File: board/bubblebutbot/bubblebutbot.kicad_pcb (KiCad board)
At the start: 2 copper layers, 30 x 70 mm, 32 parts, among them J1 Screw_Terminal_01x04, J2 Screw_Terminal_01x04, J3 Conn_01x06_Female, J4 Conn_01x06_Female, Q1 FDN336P, U1 WeMos_D1_mini, U3 TPS613222ADBV

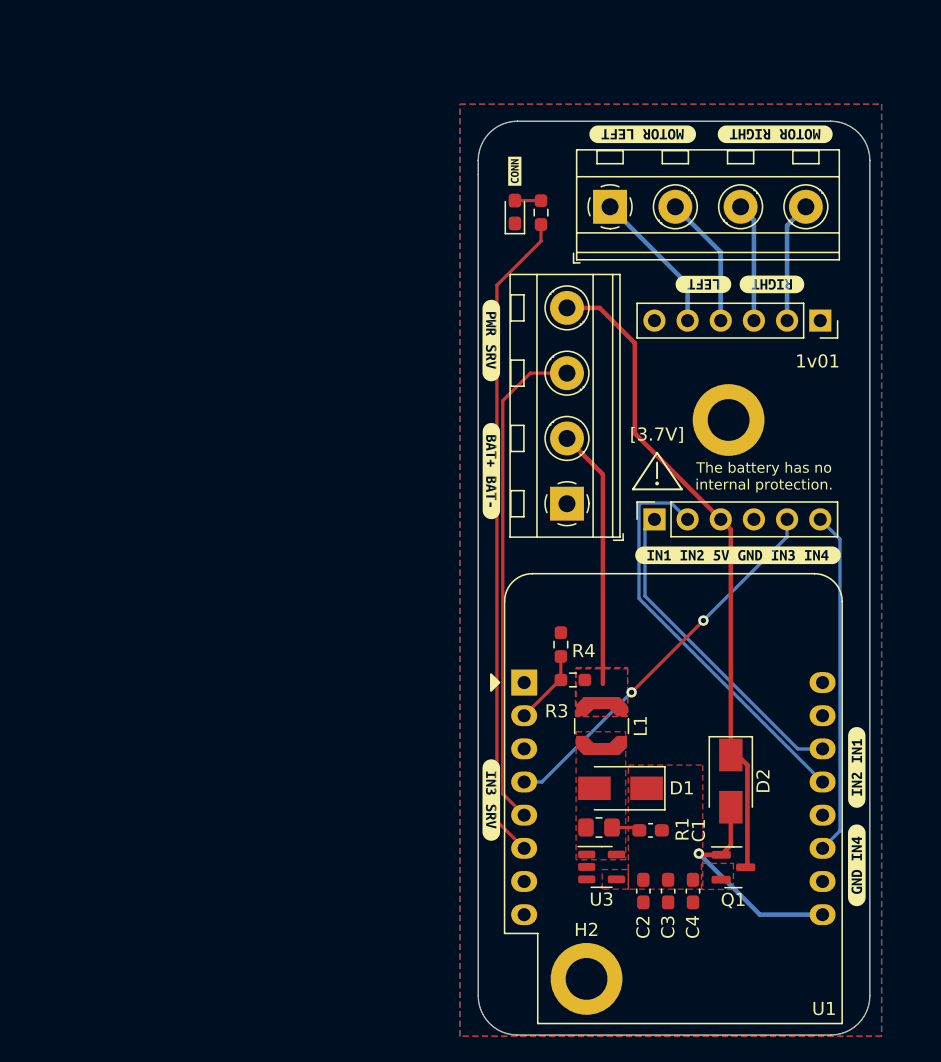
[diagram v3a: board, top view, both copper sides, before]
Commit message: finished schematic and BOM. Design is ready to start!
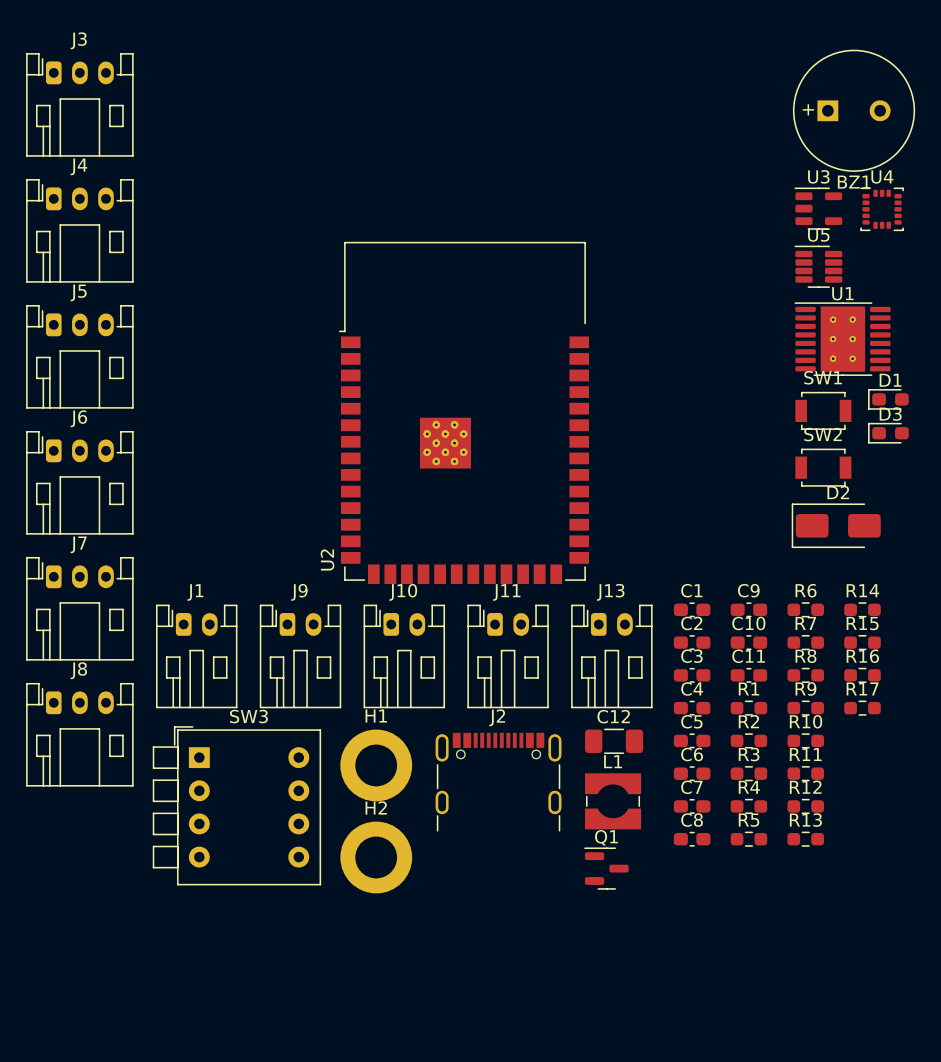
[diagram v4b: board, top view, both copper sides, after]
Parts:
- removed kibuzzard-641EE450: G***, kibuzzard-641EE450
- removed kibuzzard-641EE46F: G***, kibuzzard-641EE46F
- removed kibuzzard-641EE492: G***, kibuzzard-641EE492
- removed kibuzzard-641EE4C6: G***, kibuzzard-641EE4C6
- removed kibuzzard-641EE536: G***, kibuzzard-641EE536
- removed kibuzzard-641EE568: G***, kibuzzard-641EE568
- removed kibuzzard-641EE5F8: G***, kibuzzard-641EE5F8
- removed kibuzzard-641EE609: G***, kibuzzard-641EE609
- removed kibuzzard-641EE6B8: G***, kibuzzard-641EE6B8
- removed kibuzzard-641EE6C6: G***, kibuzzard-641EE6C6
- removed kibuzzard-641EE74D: G***, kibuzzard-641EE74D
- added BZ1: Buzzer, Buzzer_Beeper:MagneticBuzzer_PUI_AT-0927-TT-6-R, F.Cu at (177.8, 73.2)
- added C10: 10u, Capacitor_SMD:C_0603_1608Metric_Pad1.08x0.95mm_HandSolder, F.Cu at (171.7, 113.9)
- added C11: 100n, Capacitor_SMD:C_0603_1608Metric_Pad1.08x0.95mm_HandSolder, F.Cu at (171.7, 116.5)
- added C12: 22u, Capacitor_SMD:C_1206_3216Metric_Pad1.33x1.80mm_HandSolder, F.Cu at (161.4, 121.5)
- added C5: 1u, Capacitor_SMD:C_0603_1608Metric_Pad1.08x0.95mm_HandSolder, F.Cu at (167.4, 121.5)
- added C6: 100n, Capacitor_SMD:C_0603_1608Metric_Pad1.08x0.95mm_HandSolder, F.Cu at (167.4, 124.0)
- added C7: 2.2u, Capacitor_SMD:C_0603_1608Metric_Pad1.08x0.95mm_HandSolder, F.Cu at (167.4, 126.5)
- added C8: 100n, Capacitor_SMD:C_0603_1608Metric_Pad1.08x0.95mm_HandSolder, F.Cu at (167.4, 129.0)
- added C9: 10u, Capacitor_SMD:C_0603_1608Metric_Pad1.08x0.95mm_HandSolder, F.Cu at (171.7, 111.4)
- added J10: JST XH, Connector_JST:JST_PH_S2B-PH-K_1x02_P2.00mm_Horizontal, F.Cu at (144.3, 112.5)
- added J11: JST XH, Connector_JST:JST_PH_S2B-PH-K_1x02_P2.00mm_Horizontal, F.Cu at (152.3, 112.5)
- added J13: JST XH, Connector_JST:JST_PH_S2B-PH-K_1x02_P2.00mm_Horizontal, F.Cu at (160.2, 112.5)
- added J5: Conn_01x03_Socket, Connector_JST:JST_PH_S3B-PH-K_1x03_P2.00mm_Horizontal, F.Cu at (118.5, 89.6)
- added J6: Conn_01x03_Socket, Connector_JST:JST_PH_S3B-PH-K_1x03_P2.00mm_Horizontal, F.Cu at (118.5, 99.2)
- added J7: Conn_01x03_Socket, Connector_JST:JST_PH_S3B-PH-K_1x03_P2.00mm_Horizontal, F.Cu at (118.5, 108.9)
- added J8: Conn_01x03_Socket, Connector_JST:JST_PH_S3B-PH-K_1x03_P2.00mm_Horizontal, F.Cu at (118.5, 118.5)
- added J9: JST XH, Connector_JST:JST_PH_S2B-PH-K_1x02_P2.00mm_Horizontal, F.Cu at (136.4, 112.5)
- added R10: 5.1K, Resistor_SMD:R_0603_1608Metric_Pad0.98x0.95mm_HandSolder, F.Cu at (176.1, 121.5)
- added R11: 50k, Resistor_SMD:R_0603_1608Metric_Pad0.98x0.95mm_HandSolder, F.Cu at (176.1, 124.0)
- added R12: 5.1K, Resistor_SMD:R_0603_1608Metric_Pad0.98x0.95mm_HandSolder, F.Cu at (176.1, 126.5)
- added R13: 5.1K, Resistor_SMD:R_0603_1608Metric_Pad0.98x0.95mm_HandSolder, F.Cu at (176.1, 129.0)
- added R14: 100k, Resistor_SMD:R_0603_1608Metric_Pad0.98x0.95mm_HandSolder, F.Cu at (180.4, 111.4)
- added R15: 100k, Resistor_SMD:R_0603_1608Metric_Pad0.98x0.95mm_HandSolder, F.Cu at (180.4, 113.9)
- added R16: R, Resistor_SMD:R_0603_1608Metric_Pad0.98x0.95mm_HandSolder, F.Cu at (180.4, 116.5)
- added R17: 5.1K, Resistor_SMD:R_0603_1608Metric_Pad0.98x0.95mm_HandSolder, F.Cu at (180.4, 119.0)
- added R5: 3.3k, Resistor_SMD:R_0603_1608Metric_Pad0.98x0.95mm_HandSolder, F.Cu at (171.7, 129.0)
- added R6: 5.1K, Resistor_SMD:R_0603_1608Metric_Pad0.98x0.95mm_HandSolder, F.Cu at (176.1, 111.4)
- added R7: 5.1K, Resistor_SMD:R_0603_1608Metric_Pad0.98x0.95mm_HandSolder, F.Cu at (176.1, 113.9)
- added R8: 100k, Resistor_SMD:R_0603_1608Metric_Pad0.98x0.95mm_HandSolder, F.Cu at (176.1, 116.5)
- added R9: 5.1K, Resistor_SMD:R_0603_1608Metric_Pad0.98x0.95mm_HandSolder, F.Cu at (176.1, 119.0)
- added SW1: SW_Push, Button_Switch_SMD:SW_SPST_B3U-1000P, F.Cu at (177.4, 96.2)
- added SW2: SW_Push, Button_Switch_SMD:SW_SPST_B3U-1000P, F.Cu at (177.4, 100.5)
- added SW3: SW_DIP_x04, Button_Switch_THT:SW_DIP_SPSTx04_Piano_10.8x11.72mm_W7.62mm_P2.54mm, F.Cu at (129.6, 122.8)
- added U2: ESP32-S3-WROOM-1, RF_Module:ESP32-S3-WROOM-1, F.Cu at (150.0, 96.2)
- added U4: LIS3DH, Package_LGA:LGA-16_3x3mm_P0.5mm_LayoutBorder3x5y, F.Cu at (181.9, 80.8)
- added U5: ~, Package_TO_SOT_SMD:SOT-23-8, F.Cu at (177.1, 85.2)
- C1: value 120p -> 10u
- C4: value 10u -> 1u
- D1: value SS14 -> LED; footprint Diode_SMD:D_SMA -> LED_SMD:LED_0603_1608Metric_Pad1.05x0.95mm_HandSolder
- J1: value Screw_Terminal_01x04 -> JST XH; footprint TerminalBlock_MetzConnect:TerminalBlock_MetzConnect_Type094_RT03504HBLU_1x04_P5.00mm_Horizontal -> Connector_JST:JST_PH_S2B-PH-K_1x02_P2.00mm_Horizontal
- J2: value Screw_Terminal_01x04 -> USB_C_Receptacle; footprint TerminalBlock_MetzConnect:TerminalBlock_MetzConnect_Type094_RT03504HBLU_1x04_P5.00mm_Horizontal -> Connector_USB:USB_C_Receptacle_GCT_USB4105-xx-A_16P_TopMnt_Horizontal
- J3, J4: value Conn_01x06_Female -> Conn_01x03_Socket; footprint Connector_PinSocket_2.54mm:PinSocket_1x06_P2.54mm_Vertical -> Connector_JST:JST_PH_S3B-PH-K_1x03_P2.00mm_Horizontal
- L1: value 2.2u -> 4.7u; footprint Inductor_SMD:L_Coilcraft_LPS4018 -> Inductor_SMD:L_Wuerth_WE-TPC-3816
- R1: value 5 -> 5.1K; footprint Resistor_SMD:R_0805_2012Metric_Pad1.20x1.40mm_HandSolder -> Resistor_SMD:R_0603_1608Metric_Pad0.98x0.95mm_HandSolder
- R2: value 1k -> 5.1K
- R3: value 10k -> 5.1K
- R4: value 33k -> 5.1K
- U1: value WeMos_D1_mini -> DRV8833PWP; footprint Module:WEMOS_D1_mini_light -> Package_SO:HTSSOP-16-1EP_4.4x5mm_P0.65mm_EP3.4x5mm_Mask2.46x2.31mm_ThermalVias
- U3: value TPS613222ADBV -> AP2112K-3.3
- moved J3 61.7 mm to (118.5, 70.3), turned to 0 degrees
- moved U3 53.1 mm to (177.1, 80.7)
- moved J4 52.2 mm to (118.5, 80.0), turned to 0 degrees
- moved J2 45.4 mm to (152.6, 125.1)
- moved R2 43.5 mm to (171.7, 121.5), turned to 0 degrees
- moved H1 37.8 mm to (143.2, 123.3)
- moved D1 36.3 mm to (182.6, 95.3), turned to 0 degrees
- moved U1 35.9 mm to (178.9, 90.7)
- moved D3 33.4 mm to (182.6, 97.9), turned to 0 degrees
- moved J1 30.8 mm to (128.4, 112.5), turned to 0 degrees
- moved D2 21.2 mm to (178.6, 105.0), turned to 0 degrees
- moved C2 19.4 mm to (167.4, 113.9), turned to 0 degrees
- moved R4 19.0 mm to (171.7, 126.5), turned to 0 degrees
- moved H2 18.6 mm to (143.2, 130.4)
- moved C1 17.2 mm to (167.4, 111.4)
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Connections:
- C1 pad 1: Net-(C1-Pad1) -> +3.3V
- C1 pad 2: Net-(C1-Pad2) -> GND
- C2 pad 1: Net-(C1-Pad2) -> +3.3V
- C3 pad 1: Net-(C1-Pad2) -> ESP32-RESET
- C4 pad 1: Net-(C1-Pad2) -> +3.3V
- D1 pad 1: Net-(C1-Pad2) -> GND
- D1 pad 2: Net-(D1-Pad2) -> Net-(D1-A)
- D2 pad 1: SPLY -> +5V
- D2 pad 2: WEMOS_USB_POWER -> 5V_USB_POWER
- D3 pad 2: Net-(D3-Pad2) -> Net-(D3-A)
- J1 pad 2: Net-(L1-Pad1) -> +7.5V
- J3 pad 1: unconnected-(J3-Pad1) -> GND
- J3 pad 2: Net-(J3-Pad2) -> ESP32-IR-FL
- J3 pad 3: Net-(J3-Pad3) -> +5V
- J4 pad 1: IN1 -> GND
- J4 pad 2: IN2 -> ESP32-IR-FR
- J4 pad 3: SPLY -> +5V
- L1 pad 1: Net-(L1-Pad1) -> Net-(U5-LX)
- L1 pad 2: Net-(D1-Pad2) -> 5V_BAT
- Q1 pad 1: WEMOS_USB_POWER -> 5V_USB_POWER
- Q1 pad 2: Net-(C1-Pad2) -> 5V_BAT
- Q1 pad 3: SPLY -> +5V
- R1 pad 1: Net-(D1-Pad2) -> +3.3V
- R1 pad 2: Net-(C1-Pad1) -> ESP32-RESET
- R2 pad 1: Net-(R2-Pad1) -> Net-(D1-A)
- R2 pad 2: Net-(D3-Pad2) -> ESP32-OP-LED
- R3 pad 1: Net-(L1-Pad1) -> Net-(R3-Pad1)
- R3 pad 2: BATTERY_LVL -> +3.3V
- R4 pad 1: BATTERY_LVL -> GND
- R4 pad 2: GND -> Net-(J2-CC1)
- U1 pad 1: unconnected-(U1-Pad1) -> Net-(U1-nSLEEP)
- U1 pad 10: GND -> ESP32-MOTOR-BIN2
- U1 pad 11: IN4 -> Net-(U1-VCP)
- U1 pad 12: unconnected-(U1-Pad12) -> 5V_SUPPLY
- U1 pad 13: IN2 -> GND
- U1 pad 14: IN1 -> Net-(U1-VINT)
- U1 pad 15: unconnected-(U1-Pad15) -> ESP32-MOTOR-AIN2
- U1 pad 16: unconnected-(U1-Pad16) -> ESP32-MOTOR-AIN1
- U1 pad 2: BATTERY_LVL -> MOTOR-RIGHT-BL
- U1 pad 3: unconnected-(U1-Pad3) -> GND
- U1 pad 4: IN3 -> MOTOR-RIGHT-BR
- U1 pad 5: SERVO_PWM -> MOTOR-LEFT-BR
- U1 pad 6: Net-(R2-Pad1) -> GND
- U1 pad 7: unconnected-(U1-Pad7) -> MOTOR-LEFT-BL
- U1 pad 8: unconnected-(U1-Pad8) -> ESP32-MOTOR-FAULT
- U1 pad 9: WEMOS_USB_POWER -> ESP32-MOTOR-BIN1
- U3 pad 1: Net-(D1-Pad2) -> +5V
- U3 pad 3: unconnected-(U3-Pad3) -> +5V
- U3 pad 4: Net-(C1-Pad2) -> unconnected-(U3-NC-Pad4)
- U3 pad 5: unconnected-(U3-Pad5) -> +3.3V
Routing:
- net SPLY: track 50.1 -> 0.00 mm
- net Net-(R2-Pad1): track 50.1 -> 0.00 mm
- net SERVO_PWM: track 38.2 -> 0.00 mm
- net IN2: track 31.4 -> 0.00 mm
- net IN3: track 29.3 -> 0.00 mm, vias 2 -> 0
- net IN4: track 26.4 -> 0.00 mm
- net IN1: track 24.6 -> 0.00 mm
- net Net-(L1-Pad1): track 19.9 -> 0.00 mm
- net WEMOS_USB_POWER: track 16.9 -> 0.00 mm, vias 1 -> 0
- net Net-(J3-Pad5): track 11.2 -> 0.00 mm
- net Net-(J3-Pad4): track 10.2 -> 0.00 mm
- net Net-(J3-Pad2): track 9.32 -> 0.00 mm
- net Net-(J3-Pad3): track 9.14 -> 0.00 mm
- net BATTERY_LVL: track 5.75 -> 0.00 mm
- net Net-(C1-Pad1): track 2.18 -> 0.00 mm
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- removed copper zone on B.Cu, net GND
- removed copper zone on F.Cu, net GND
- removed copper zone on F.Cu, net Net-(C1-Pad2)
- removed copper zone on F.Cu, net Net-(D1-Pad2)
- removed copper zone on F.Cu, net Net-(L1-Pad1)
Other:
- board outline removed
- board text removed: "1v01"
- board text removed: "The battery has no internal protection."
- board text removed: "[3.7V]"

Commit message: a few more improvements here and there. Almost there.
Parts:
- removed R3: 5.1K, Resistor_SMD:R_0603_1608Metric_Pad0.98x0.95mm_HandSolder
- removed SW3: SW_DIP_x04, Button_Switch_THT:SW_DIP_SPSTx04_Piano_10.8x11.72mm_W7.62mm_P2.54mm
- moved R17 140.8 mm to (72.4, 28.6)
- moved D3 133.5 mm to (68.5, 28.6)
- moved R4 129.7 mm to (77.1, 37.8), turned to 90 degrees
- moved R10 128.2 mm to (78.9, 37.8), turned to 90 degrees
- moved R13 128.0 mm to (76.6, 48.4), turned to 90 degrees
- moved R7 126.3 mm to (75.3, 37.8), turned to -90 degrees
- moved Q1 122.9 mm to (82.2, 36.9)
- moved J2 122.6 mm to (69.3, 35.1), turned to -90 degrees
- moved R15 122.5 mm to (81.2, 42.2), turned to 180 degrees
- moved R16 120.8 mm to (85.2, 42.2)
- moved R5 119.5 mm to (80.3, 52.0), turned to -90 degrees
- moved D2 119.0 mm to (83.8, 33.1), turned to 180 degrees
- moved L1 118.0 mm to (76.6, 43.9), turned to 180 degrees
- moved C5 117.6 mm to (88.5, 34.3), turned to -90 degrees
- moved H1 117.0 mm to (78.5, 25.8)
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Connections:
- R8 pad 2: +5V -> Net-(U3-EN)
- U2 pad 12: ESP32-SRV-F -> unconnected-(U2-GPIO8/TOUCH8/ADC1_CH7/SUBSPICS1-Pad12)
- U2 pad 18: ESP32-OP-LED -> ESP32-SRV-F
- U2 pad 19: ESP32-WIFI-ANALOG -> ESP32-OP-LED
- U2 pad 20: ESP32-MANUAL-AUTO -> ESP32-ACC-SDA
- U2 pad 21: ESP32-SERVO-EN -> ESP32-ACC-SCL
- U3 pad 3: +5V -> Net-(U3-EN)
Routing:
- net MOTOR-LEFT-BR: track 0.00 -> 15.5 mm, vias 0 -> 1
- net MOTOR-LEFT-BL: track 0.00 -> 15.1 mm
- net ESP32-ACC-INT1: track 0.00 -> 13.4 mm, vias 0 -> 2
- net ESP32-ACC-INT2: track 0.00 -> 12.3 mm, vias 0 -> 2
- net ESP32-ACC-SCL: track 0.00 -> 11.8 mm
- net ESP32-IR-BR: track 0.00 -> 10.8 mm, vias 0 -> 1
- net ESP32-IR-BL: track 0.00 -> 10.7 mm, vias 0 -> 1
- net ESP32-ACC-SDA: track 0.00 -> 10.1 mm
- net ESP32-IR-FL: track 0.00 -> 1.97 mm, vias 0 -> 1
- net ESP32-IR-FR: track 0.00 -> 1.97 mm, vias 0 -> 1
- added copper zone on F.Cu, net GND
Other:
- board outline added: 94 x 32.5 mm
- board text added: "power.bat"
- board text added: "power.usb"

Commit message: pcb done!
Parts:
- added kibuzzard-6507374A: G***, kibuzzard-6507374A, F.Cu at (115.5, 33.6)
- added kibuzzard-6507377B: G***, kibuzzard-6507377B, F.Cu at (124.0, 33.6)
- added kibuzzard-65073792: G***, kibuzzard-65073792, F.Cu at (133.6, 33.6)
- added kibuzzard-650737FA: G***, kibuzzard-650737FA, F.Cu at (143.0, 33.6)
- added kibuzzard-65073803: G***, kibuzzard-65073803, F.Cu at (151.5, 33.6)
- added kibuzzard-65073819: G***, kibuzzard-65073819, F.Cu at (115.5, 44.5)
- added kibuzzard-6507382A: G***, kibuzzard-6507382A, F.Cu at (124.0, 44.5)
- added kibuzzard-6507384E: G***, kibuzzard-6507384E, F.Cu at (133.5, 44.5)
- added kibuzzard-6507385B: G***, kibuzzard-6507385B, F.Cu at (143.0, 44.5)
- added kibuzzard-65073881: G***, kibuzzard-65073881, F.Cu at (151.5, 44.5)
- added kibuzzard-650738AB: G***, kibuzzard-650738AB, F.Cu at (135.3, 36.6)
- added kibuzzard-650739D2: G***, kibuzzard-650739D2, F.Cu at (69.3, 44.4)
- added kibuzzard-650739DD: G***, kibuzzard-650739DD, F.Cu at (66.4, 42.8)
- added kibuzzard-650739F6: G***, kibuzzard-650739F6, F.Cu at (66.3, 27.5)
- moved C1 43.1 mm to (108.8, 52.0), turned to -90 degrees
- moved D1 42.2 mm to (99.4, 28.1)
- moved R2 42.2 mm to (99.4, 31.8)
- moved U2 41.9 mm to (97.8, 47.4)
- moved C6 41.5 mm to (90.2, 27.1), turned to -90 degrees
- moved C2 41.4 mm to (110.6, 52.0), turned to -90 degrees
- moved R12 40.0 mm to (93.8, 27.1), turned to 90 degrees
- moved C10 39.8 mm to (92.0, 27.1), turned to -90 degrees
- moved U4 39.2 mm to (94.6, 31.6), turned to -90 degrees
- moved R9 35.2 mm to (95.6, 27.1)
- moved C3 33.3 mm to (122.8, 42.6), turned to -90 degrees
- moved R1 31.5 mm to (120.8, 42.6), turned to 90 degrees
- moved J10 28.6 mm to (116.5, 31.1)
- moved J13 28.6 mm to (152.5, 31.1)
- moved J3 28.6 mm to (126.0, 31.1)
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- renumbered SW2 to boot, SW1 to rst
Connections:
- C8 pad 2: 5V_SUPPLY -> +5V
- R11 pad 1: 5V_SUPPLY -> +5V
- U1 pad 12: 5V_SUPPLY -> +5V
- U2 pad 10: ESP32-MOTOR-AIN1 -> ESP32-SRV-B
- U2 pad 11: ESP32-MOTOR-AIN2 -> ESP32-SRV-F
- U2 pad 17: ESP32-SRV-B -> ESP32-MOTOR-AIN1
- U2 pad 18: ESP32-SRV-F -> ESP32-MOTOR-AIN2
- U2 pad 19: ESP32-OP-LED -> ESP32-MOTOR-BIN1
- U2 pad 20: ESP32-ACC-SDA -> ESP32-MOTOR-FAULT
- U2 pad 21: ESP32-ACC-SCL -> ESP32-OP-LED
- U2 pad 22: ESP32-MOTOR-FAULT -> ESP32-ACC-INT1
- U2 pad 23: ESP32-MOTOR-BIN1 -> ESP32-ACC-INT2
- U2 pad 24: ESP32-ACC-INT1 -> ESP32-ACC-SDA
- U2 pad 25: ESP32-ACC-INT2 -> ESP32-ACC-SCL
- U2 pad 4: ESP32-IR-FL -> ESP32-IR-BR
- U2 pad 5: ESP32-IR-FR -> ESP32-IR-BL
- U2 pad 6: ESP32-IR-BL -> ESP32-IR-FR
- U2 pad 7: ESP32-IR-BR -> ESP32-IR-FL
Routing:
- net +5V: track 0.00 -> 97.7 mm, vias 0 -> 5
- net ESP32-BUZZER: track 0.00 -> 70.4 mm, vias 0 -> 1
- net MOTOR-RIGHT-BL: track 0.00 -> 61.0 mm
- net MOTOR-RIGHT-BR: track 0.00 -> 60.7 mm
- net ESP32-D+: track 0.00 -> 46.8 mm, vias 0 -> 2
- net +3.3V: track 0.00 -> 45.9 mm, vias 0 -> 7
- net ESP32-BOOT0: track 0.00 -> 44.4 mm, vias 0 -> 2
- net ESP32-D-: track 0.00 -> 41.9 mm, vias 0 -> 2
- net ESP32-IR-FR: track 1.97 -> 42.6 mm, vias 1 -> 0
- net ESP32-SRV-F: track 0.00 -> 31.2 mm, vias 0 -> 1
- net ESP32-SRV-B: track 0.00 -> 30.0 mm, vias 0 -> 1
- net ESP32-IR-BR: track 10.8 -> 38.9 mm, vias 1 -> 2
- net ESP32-MOTOR-BIN2: track 0.00 -> 27.5 mm, vias 0 -> 2
- net ESP32-RESET: track 0.00 -> 25.1 mm, vias 0 -> 2
- net ESP32-IR-FL: track 1.97 -> 25.0 mm, vias 1 -> 0
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- added copper zone on F.Cu, net +3.3V
- added copper zone on F.Cu, net +5V
- added copper zone on F.Cu, net +7.5V
- added copper zone on F.Cu, net 5V_BAT
- added copper zone on F.Cu, net 5V_USB_POWER
- added copper zone on B.Cu, net GND
- added copper zone on F.Cu, net Net-(U5-FB)
- added copper zone on F.Cu, net Net-(U5-LX)
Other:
- board size 94 x 32.5 mm -> 90 x 30 mm
- board text removed: "power.bat"
- board text removed: "power.usb"
